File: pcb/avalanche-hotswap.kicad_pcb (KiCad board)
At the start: 2 copper layers, 179.4 x 124.3 mm, 129 parts, among them J1 TRRS, P1 i2c_pin, P2 i2c_pin, P3 battery+, P4 battery-, SW0 SW_Push, SW1 SW_Push, SW10 SW_Push, SW11 SW_Push, SW12 SW_Push, SW13 SW_Push, SW14 SW_Push, SW15 SW_Push, SW16 SW_Push, SW17 SW_Push, SW18 SW_Push, SW19 SW_Push, SW2 SW_Push, SW20 SW_Push, SW21 SW_Push, SW22 SW_Push, SW23 SW_Push, SW24 SW_Push, SW25 SW_Push, SW26 SW_Push, SW27 SW_Push, SW28 SW_Push, SW29 SW_Push, SW3 SW_Push, SW30 SW_Push, SW31 SW_Push, SW32 SW_Push, SW33 SW_DPDT_x2, SW34 SW_DPDT_x2, SW4 SW_Push, SW5 SW_Push, SW6 SW_Push, SW7 SW_Push, SW8 SW_Push, SW9 SW_Push, U1 ProMicro

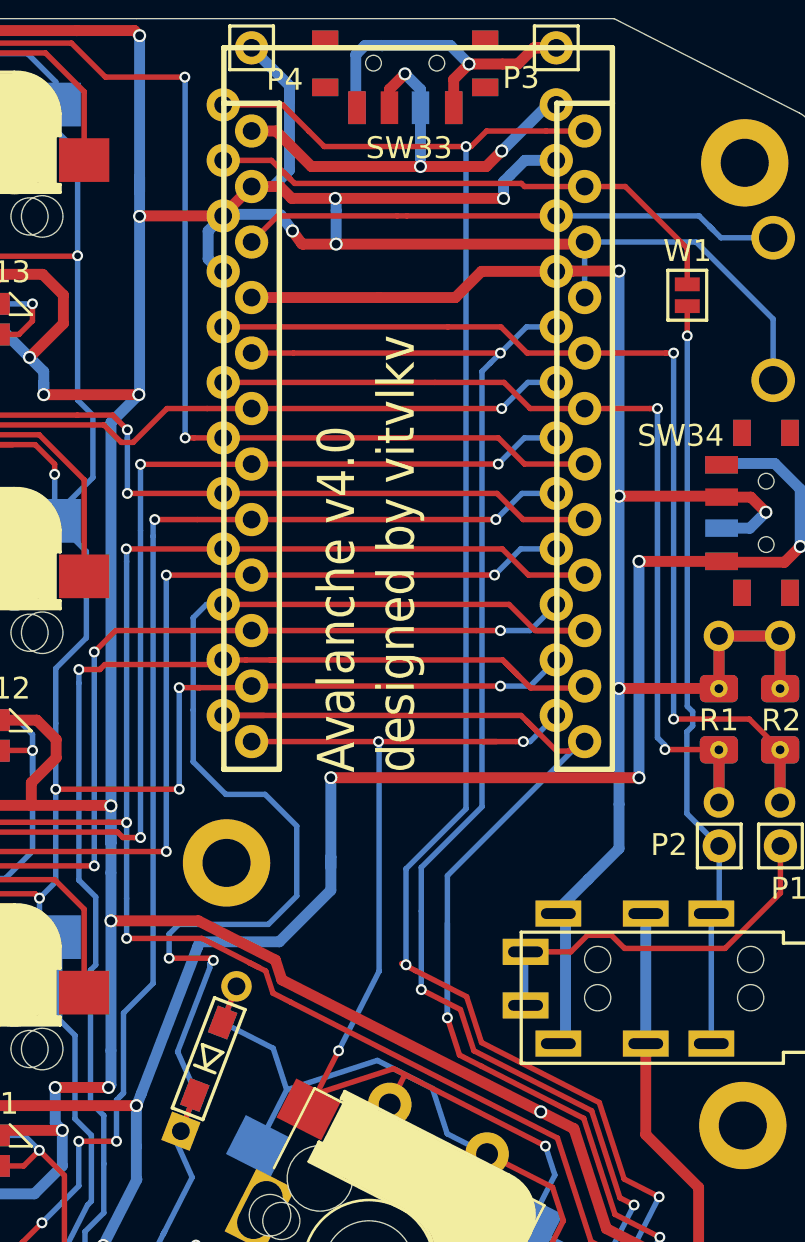
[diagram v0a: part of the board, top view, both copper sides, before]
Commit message: Added wide horizontal OLED SSD1306
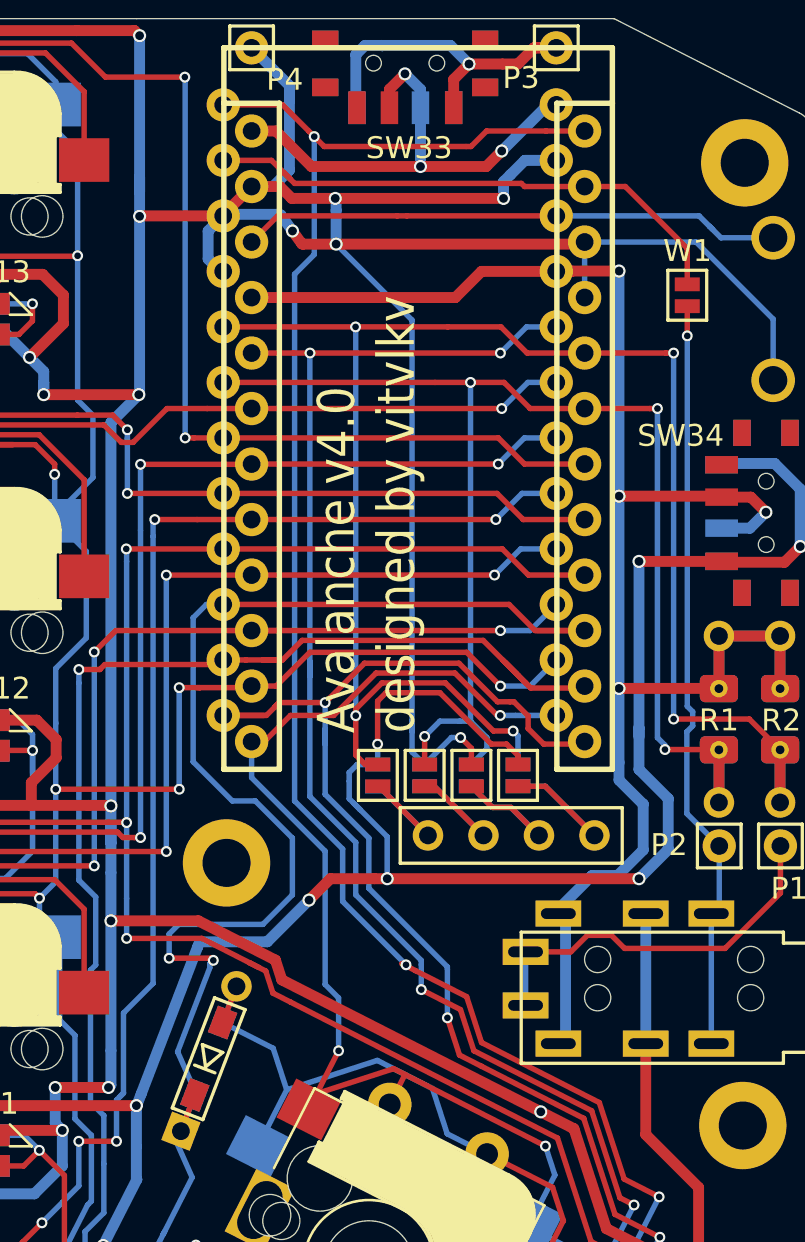
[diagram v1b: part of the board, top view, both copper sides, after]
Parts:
- added J2: OLED, used_footprints:OLED_4Pin_SSD1306, B.Cu at (207.8, 92.8)
- added JP1: Device_Jumper_NO_Small, used_footprints:avalanche_Jumper, B.Cu at (201.7, 90.0)
- added JP2: Device_Jumper_NO_Small, used_footprints:avalanche_Jumper, B.Cu at (203.8, 90.0)
- added JP3: Device_Jumper_NO_Small, used_footprints:avalanche_Jumper, B.Cu at (206.0, 90.0)
- added JP4: Device_Jumper_NO_Small, used_footprints:avalanche_Jumper, B.Cu at (208.1, 90.0)
- added JP5: Device_Jumper_NO_Small, used_footprints:avalanche_Jumper, F.Cu at (201.7, 90.0)
- added JP6: Device_Jumper_NO_Small, used_footprints:avalanche_Jumper, F.Cu at (203.9, 90.0)
- added JP7: Device_Jumper_NO_Small, used_footprints:avalanche_Jumper, F.Cu at (206.0, 90.0)
- added JP8: Device_Jumper_NO_Small, used_footprints:avalanche_Jumper, F.Cu at (208.1, 90.0)
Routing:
- net SDA: track 48.2 -> 79.5 mm, vias 2 -> 5
- net GND: track 1131.0 -> 1160.5 mm, vias 79 -> 80
- net SCL: track 43.4 -> 65.2 mm, vias 2 -> 4
- net VCC: track 966.5 -> 985.7 mm, vias 61 -> 63
- net Net-(J2-Pad1): track 0.00 -> 8.86 mm
- net Net-(J2-Pad2): track 0.00 -> 8.05 mm
- net Net-(J2-Pad3): track 0.00 -> 7.25 mm
- net Net-(J2-Pad4): track 0.00 -> 6.45 mm
- net col6: track 131.7 -> 134.4 mm, vias 10 -> 9
- net row4: track 307.0 -> 309.6 mm
- net LED: track 104.6 -> 106.4 mm
- net PIN21: track 83.7 -> 85.3 mm
- net encB: track 200.7 -> 202.0 mm, vias 6 -> 7
- net col5: track 220.7 -> 222.0 mm
- net row3: track 222.6 -> 221.9 mm
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
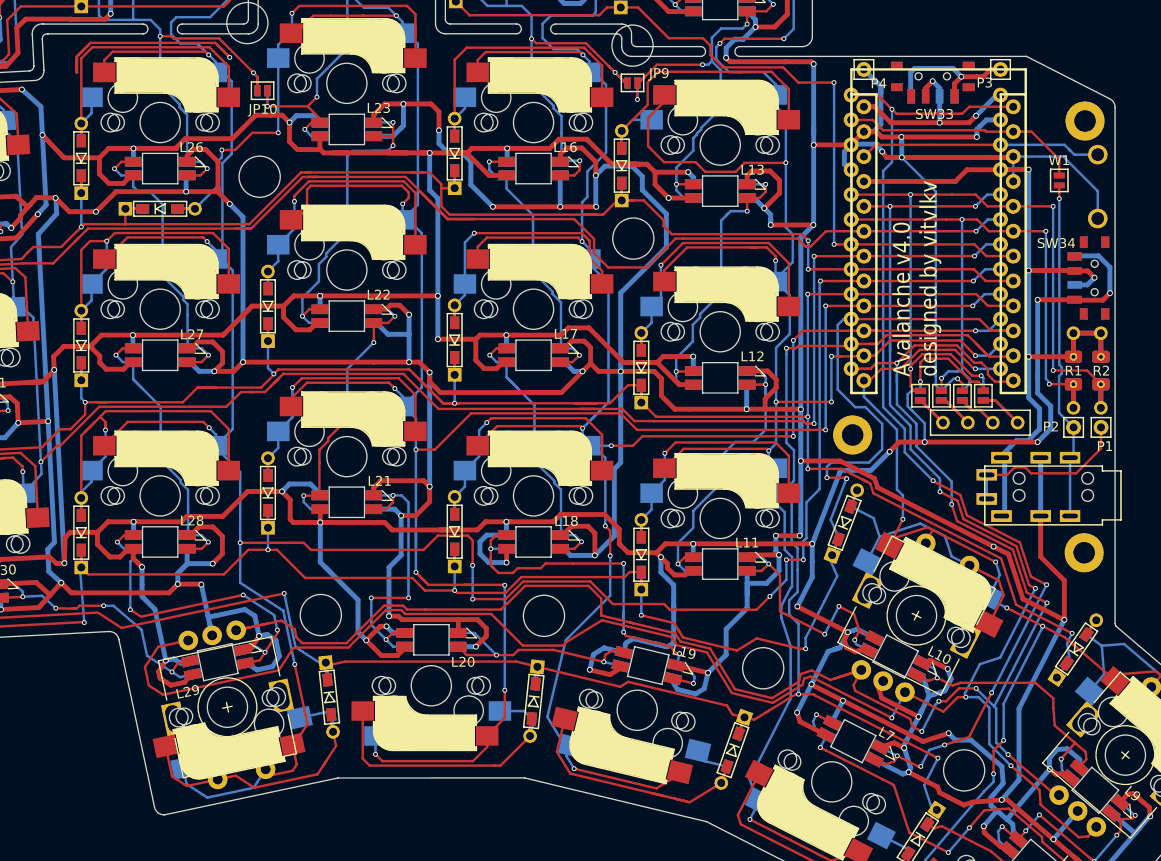
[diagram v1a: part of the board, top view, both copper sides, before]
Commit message: Rerouting
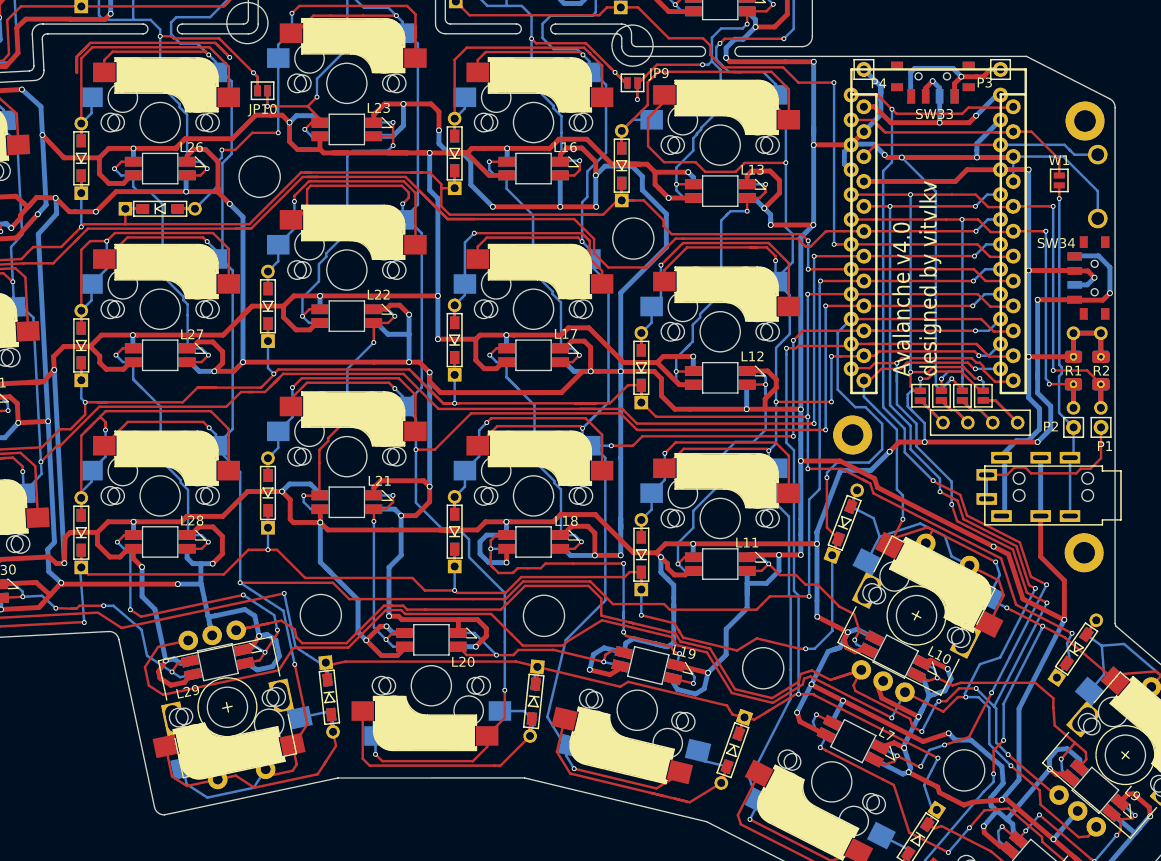
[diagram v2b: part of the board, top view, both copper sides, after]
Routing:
- net GND: track 1160.5 -> 1147.0 mm, vias 80 -> 78
- net col3: track 270.8 -> 263.0 mm, vias 12 -> 10
- net Net-(L20-Pad2): track 29.6 -> 23.1 mm, vias 4 -> 3
- net col2: track 296.2 -> 290.9 mm, vias 13 -> 9
- net Net-(L10-Pad2): track 27.6 -> 23.0 mm, vias 4 -> 2
- net VCC: track 985.7 -> 981.3 mm
- net row3: track 221.9 -> 218.2 mm, vias 7 -> 6
- net encA: track 183.6 -> 180.3 mm
- net row4: track 309.6 -> 307.3 mm
- net DATA: track 25.3 -> 26.9 mm
- net col5: track 222.0 -> 220.7 mm
- net col6: track 134.4 -> 133.3 mm
- net SDA: track 79.5 -> 78.5 mm
- net Net-(J1-Pad4): track 18.9 -> 19.4 mm
- net col4: track 229.1 -> 228.7 mm, vias 11 -> 9

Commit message: WIP
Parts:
- moved SW25 29.9 mm to (151.6, 98.8)
- moved D23 29.9 mm to (105.4, 96.2)
- moved D13 29.9 mm to (51.5, 75.3)
- moved JP7 29.9 mm to (176.3, 86.2)
- moved L26 29.9 mm to (94.4, 63.1)
- moved SW27 29.9 mm to (36.2, 86.9)
- moved L35 29.9 mm to (54.3, 69.3)
- moved SW24 29.9 mm to (132.5, 96.5)
- moved L38 29.9 mm to (36.4, 91.6)
- moved D17 29.9 mm to (124.5, 80.6)
- moved D12 29.9 mm to (141.5, 62.8)
- moved R2 29.9 mm to (190.4, 83.7)
- moved L33 29.9 mm to (72.4, 49.2)
- moved SW18 29.9 mm to (151.6, 79.7)
- moved L34 29.9 mm to (53.3, 50.2)
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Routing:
- net col6: track 133.3 -> 136.8 mm, vias 9 -> 7
- net VCC: track 981.3 -> 977.9 mm
- net Net-(L10-Pad4): track 30.6 -> 28.5 mm
- net LED: track 106.4 -> 107.7 mm, vias 7 -> 5
- net encA: track 180.3 -> 179.5 mm, vias 7 -> 6
- net encB: track 202.0 -> 201.3 mm, vias 7 -> 6
- net row4: track 307.3 -> 306.7 mm
- net GND: track 1147.0 -> 1147.1 mm, vias 78 -> 77

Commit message: Changing stagger
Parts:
- moved L11 0.30 mm to (151.6, 103.1)
- moved L13 0.30 mm to (151.6, 65.1)
- moved HM1 0.30 mm to (188.8, 57.9)
- moved L14 0.30 mm to (151.6, 46.0)
- moved SW12 0.30 mm to (151.6, 60.4)
- moved D18 0.30 mm to (143.5, 83.1)
- moved D25 0.30 mm to (143.5, 102.2)
- moved HM10 0.30 mm to (142.7, 69.9)
- moved HM2 0.30 mm to (142.6, 50.2)
- moved JP9 0.30 mm to (142.6, 54.0)
- moved L12 0.30 mm to (151.6, 84.1)
- moved SW18 0.30 mm to (151.6, 79.4)
- moved SW25 0.30 mm to (151.6, 98.5)
- moved SW6 0.30 mm to (151.6, 41.3)
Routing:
- net col4: track 228.7 -> 231.1 mm
- net Net-(D6-Pad2): track 32.3 -> 34.0 mm
- net col3: track 263.0 -> 264.4 mm
- net row4: track 306.7 -> 308.0 mm
- net GND: track 1147.1 -> 1148.3 mm
- net row0: track 192.6 -> 193.6 mm
- net VCC: track 977.9 -> 977.0 mm
- net row3: track 217.8 -> 218.5 mm
- net col5: track 220.7 -> 221.3 mm
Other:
- outline, holes or cut-outs redrawn

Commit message: Changing stagger
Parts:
- moved D16 1.50 mm to (105.4, 78.6)
- moved D23 1.50 mm to (105.4, 97.7)
- moved D4 1.50 mm to (105.4, 40.5)
- moved JP10 1.50 mm to (104.9, 56.6)
- moved L21 1.50 mm to (113.5, 98.6)
- moved L22 1.50 mm to (113.5, 79.6)
- moved L23 1.50 mm to (113.5, 60.6)
- moved L24 1.50 mm to (113.5, 41.5)
- moved SW10 1.50 mm to (113.5, 55.9)
- moved SW16 1.50 mm to (113.5, 74.9)
- moved SW23 1.50 mm to (113.5, 93.9)
- moved SW4 1.50 mm to (113.5, 36.8)
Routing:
- net Net-(L1-Pad2): track 25.1 -> 0.00 mm, vias 1 -> 0
- net row2: track 279.1 -> 271.7 mm
- net Net-(L24-Pad2): track 21.9 -> 28.1 mm
- net VCC: track 977.0 -> 971.5 mm
- net GND: track 1148.3 -> 1144.9 mm
- net col0: track 290.4 -> 287.7 mm
- net row0: track 193.6 -> 191.1 mm
- net row1: track 184.8 -> 182.4 mm
- net col3: track 264.4 -> 262.0 mm
- net Net-(JP10-Pad1): track 53.2 -> 54.7 mm
- net Net-(L20-Pad2): track 23.1 -> 22.1 mm
- net col1: track 256.5 -> 255.5 mm
- net row3: track 218.5 -> 217.7 mm
- net Net-(D10-Pad2): track 49.8 -> 49.2 mm
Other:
- board size 179.4 x 124.3 mm -> 179.4 x 122.8 mm

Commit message: Working on stagger
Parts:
- moved L14 11.4 mm to (162.8, 48.0)
- moved HM14 11.4 mm to (167.2, 116.0)
- moved JP2 11.4 mm to (185.4, 88.2)
- moved L19 11.4 mm to (155.5, 115.8)
- moved L9 11.4 mm to (201.1, 128.5)
- moved D19 11.4 mm to (199.2, 114.1)
- moved J1 11.4 mm to (201.8, 98.4)
- moved JP6 11.4 mm to (185.4, 88.2)
- moved SW11 11.4 mm to (143.8, 60.4)
- moved SW24 11.4 mm to (143.8, 98.5)
- moved SW9 11.4 mm to (105.7, 60.4)
- moved HM10 11.4 mm to (154.0, 71.9)
- moved SW32 11.4 mm to (191.8, 139.4)
- moved D3 11.4 mm to (97.6, 45.0)
- moved HM1 11.4 mm to (200.0, 59.9)
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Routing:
- net GND: track 1144.9 -> 1148.2 mm
- net Net-(L29-Pad2): track 29.9 -> 31.4 mm
- net VCC: track 971.5 -> 970.1 mm
- net row3: track 217.7 -> 216.5 mm
- net row4: track 308.0 -> 308.6 mm
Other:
- outline, holes or cut-outs redrawn

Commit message: Stagger is done
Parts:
- moved JP6 0.32 mm to (185.4, 87.9)
- moved J2 0.32 mm to (189.4, 90.7)
- moved JP1 0.32 mm to (183.2, 87.9)
- moved JP2 0.32 mm to (185.4, 87.9)
- moved JP4 0.32 mm to (189.7, 87.9)
- moved JP8 0.32 mm to (189.7, 87.9)
- moved U1 0.32 mm to (185.0, 72.0)
- moved P4 0.32 mm to (177.5, 54.6)
- moved SW33 0.32 mm to (184.5, 55.3)
- moved P3 0.32 mm to (191.4, 54.6)
- moved JP7 0.32 mm to (187.5, 87.9)
- moved JP3 0.32 mm to (187.5, 87.9)
- moved JP5 0.32 mm to (183.2, 87.9)
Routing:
- net SDA: track 78.5 -> 80.6 mm
- net col4: track 231.1 -> 232.5 mm
- net row4: track 308.6 -> 309.9 mm
- net row2: track 271.2 -> 272.5 mm
- net VCC: track 970.1 -> 971.2 mm
- net col5: track 221.3 -> 222.4 mm
- net SCL: track 64.7 -> 65.7 mm
- net DATA: track 26.9 -> 27.6 mm
- net row0: track 190.8 -> 191.4 mm
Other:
- outline, holes or cut-outs redrawn

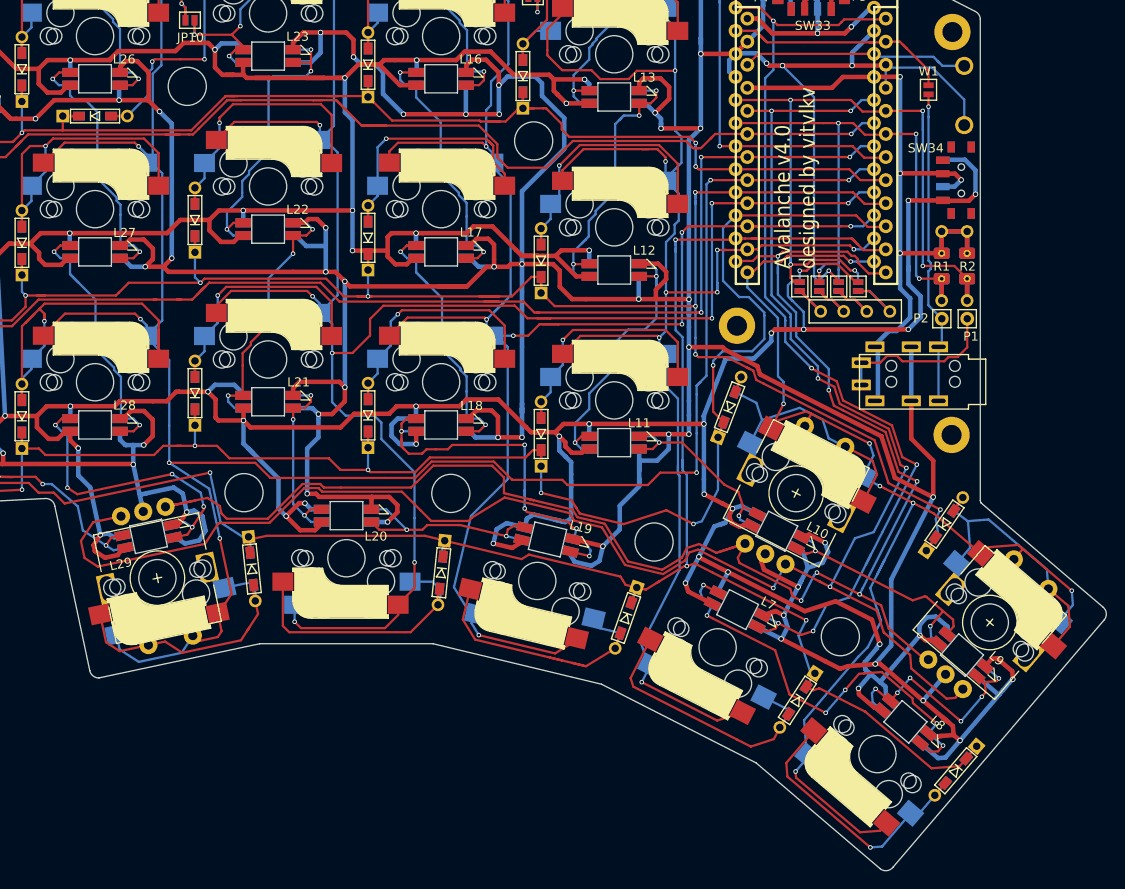
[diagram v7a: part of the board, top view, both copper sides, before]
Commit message: Moved thumb cluster up+left a bit
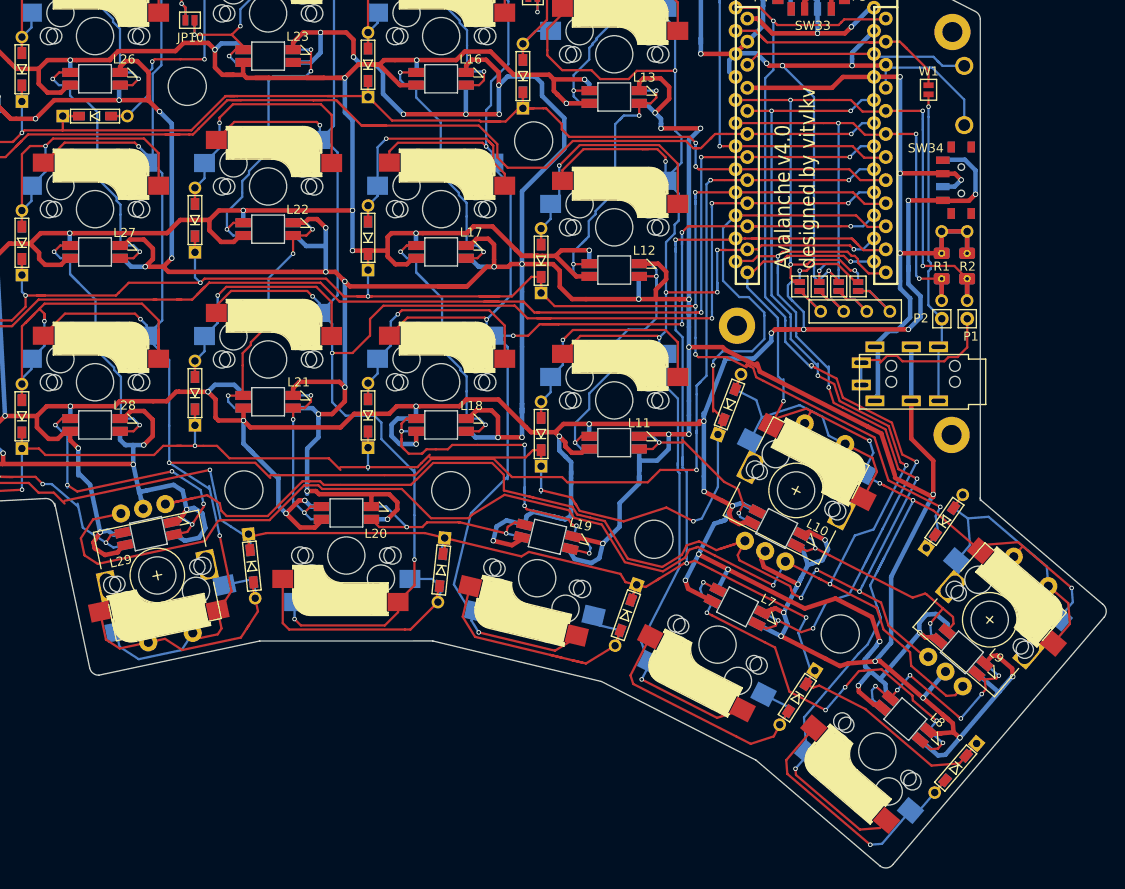
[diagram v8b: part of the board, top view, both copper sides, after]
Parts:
- moved SW31 0.30 mm to (174.2, 127.3)
- moved D31 0.30 mm to (183.0, 133.2)
- moved D32 0.30 mm to (200.4, 140.9)
- moved L8 0.30 mm to (194.9, 135.5)
- moved SW30 0.30 mm to (154.3, 120.0)
- moved HM4 0.30 mm to (144.8, 110.4)
- moved D28 0.30 mm to (122.9, 118.7)
- moved HM13 0.30 mm to (122.1, 110.3)
- moved L29 0.30 mm to (111.5, 115.1)
- moved D19 0.30 mm to (199.2, 113.8)
- moved D26 0.30 mm to (175.5, 100.9)
- moved D29 0.30 mm to (143.8, 119.1)
- moved D30 0.30 mm to (164.1, 124.1)
- moved ENC1 0.30 mm to (204.2, 124.6)
- moved ENC2 0.30 mm to (182.8, 110.4)
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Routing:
- net GND: track 1148.2 -> 1140.3 mm
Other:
- board size 179.4 x 122.8 mm -> 179.4 x 122.5 mm
